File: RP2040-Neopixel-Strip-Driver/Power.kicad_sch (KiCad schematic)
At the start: 0 parts

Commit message: Moved USB and 3.3V Regulator from RP2040 to Power Sheet
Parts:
- added C?: 10uF, Breadstick Footprints:Perfect_0402_Cap, symbol Device:C_Small
- added D? (x2): ESD_TVS, Breadstick Footprints:Perfect_0402_Resistor, symbol Device:D_TVS_Filled
- added F?: 1.5A, 3A Trip, Resistor_SMD:R_0805_2012Metric, symbol Device:Polyfuse
- added J?: TYPE-C-31-M-12, TYPE-C-31-M-12:HRO_TYPE-C-31-M-12, symbol TYPE-C-31-M-12:TYPE-C-31-M-12
- added R? (x2): 5k1, Breadstick Footprints:Perfect_0402_Resistor, symbol Device:R
- added U?: XC6206P332MR, Package_TO_SOT_SMD:SOT-23, symbol BreadstickLibrary:AZ1117R-3.3TRE1
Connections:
- new net: D?.2 (A2), D?.2 (A2), F?.2, J?.A4B9 (VBUS), J?.B4A9 (VBUS)
- new net: J?.S1 (SHIELD), J?.S2 (SHIELD), J?.S3 (SHIELD), J?.S4 (SHIELD)
- new net +3V3: U?.2 (OUT)
- new net CC1: J?.A5 (CC1), R?.2
- new net CC2: J?.B5 (CC2), R?.1
- new net GND: C?.2, D?.1 (A1), D?.1 (A1), J?.A1B12 (GND), J?.B1A12 (GND), R?.1, R?.2, U?.1 (GND)
- new net USB_D+: J?.A6 (DP1), J?.B6 (DP2)
- new net USB_D-: J?.A7 (DN1), J?.B7 (DN2)
- new net VBUS: C?.1, F?.1, U?.3 (IN)
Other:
- note added: "Placed close to uC decoupling caps."
- note added: "USB-C"

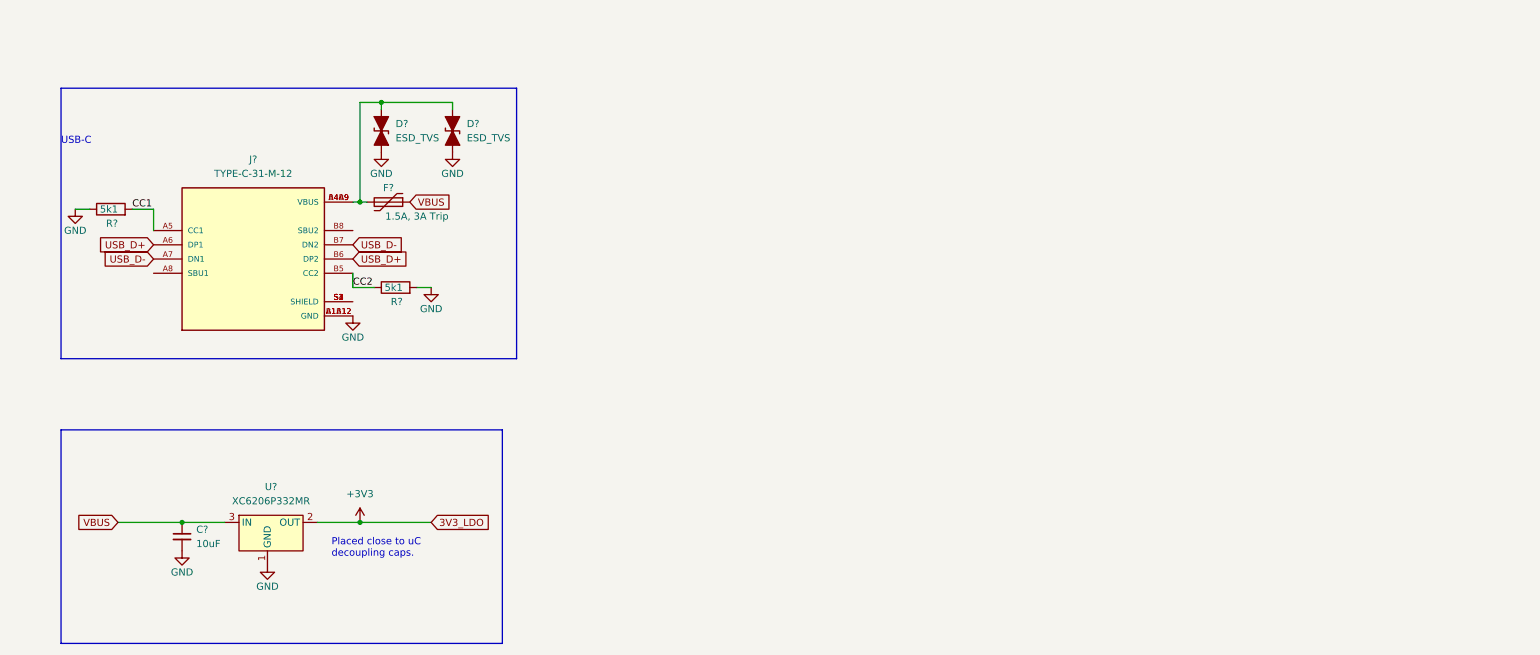
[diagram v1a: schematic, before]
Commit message: Reworked the USB-C Connector Symbol to clean up schematic
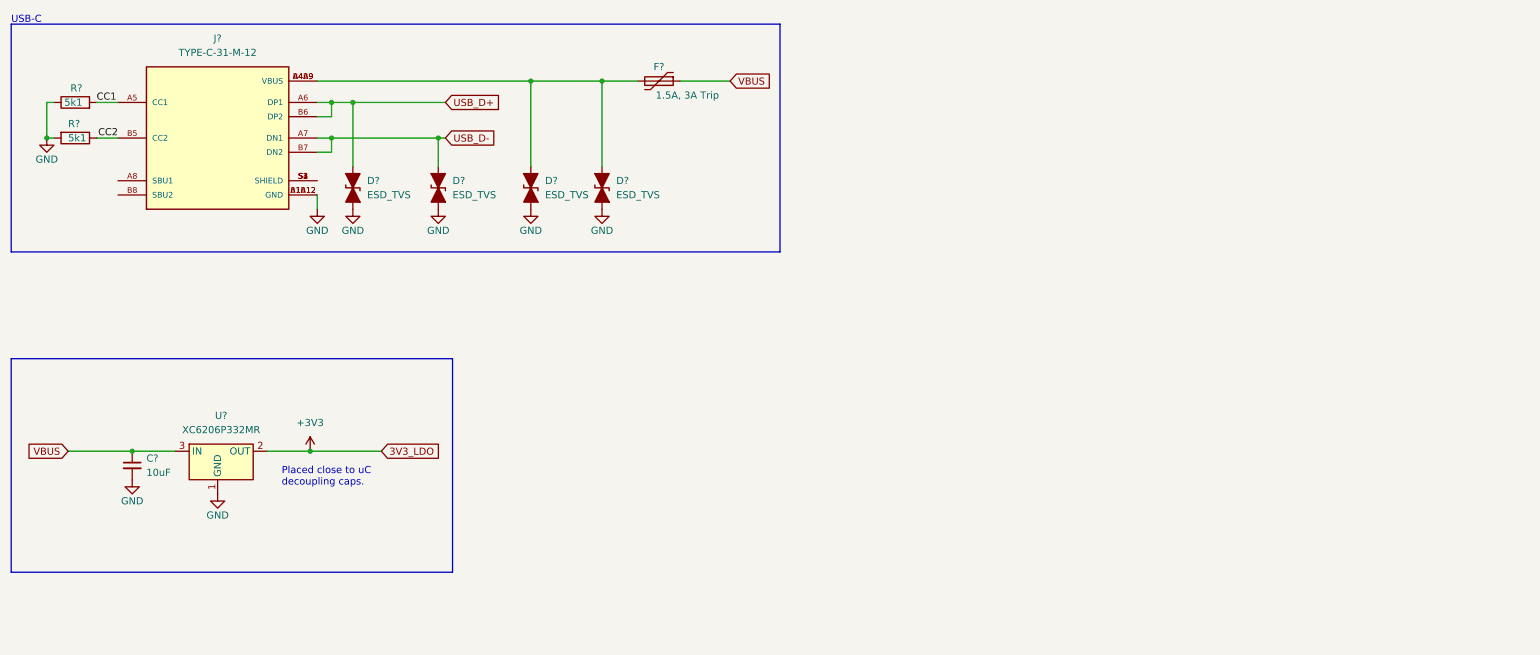
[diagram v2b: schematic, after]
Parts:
- added D? (x2): ESD_TVS, Breadstick Footprints:Perfect_0402_Resistor, symbol Device:D_TVS_Filled
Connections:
- net GND: now also D?.1 (A1), D?.1 (A1)
- net USB_D+: now also D?.2 (A2)
- net USB_D-: now also D?.2 (A2)
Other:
- moved on the sheet: C?, D?, F?, J?, R?, U?

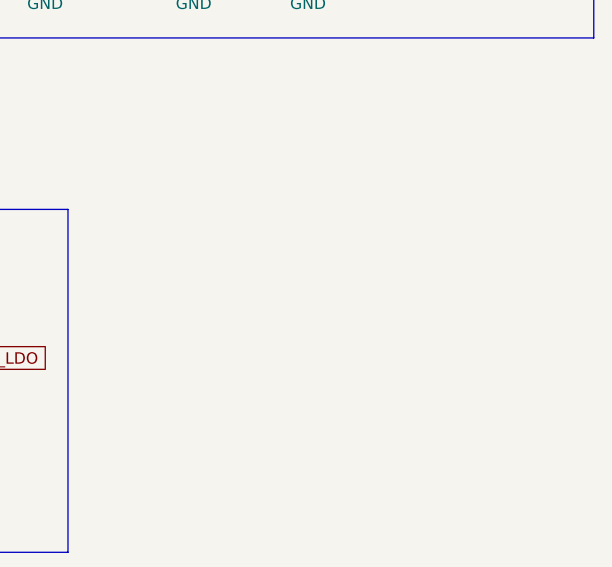
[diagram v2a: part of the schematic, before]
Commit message: Removed unnecessary pwr and gnd pins, moved decoupling caps to power sheet
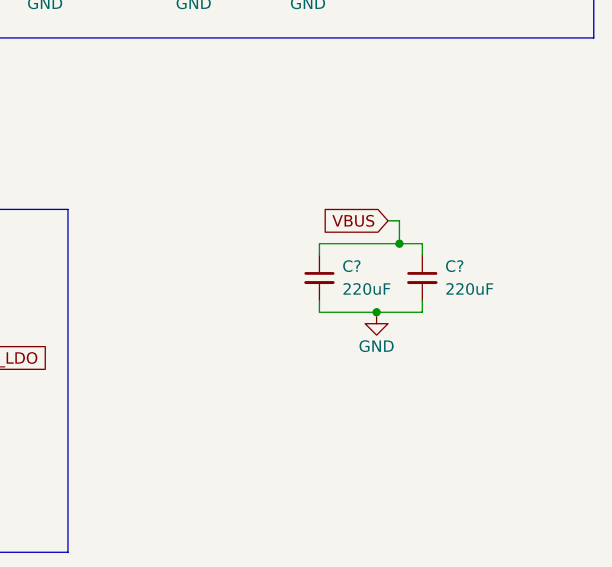
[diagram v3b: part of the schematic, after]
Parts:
- added C? (x2): 220uF, Capacitor_SMD:C_1210_3225Metric, symbol Device:C_Small
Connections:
- net GND: now also C?.2, C?.2
- net VBUS: now also C?.1, C?.1
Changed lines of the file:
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@@
   (junction (at 91.44 38.1) (diameter 0) (color 0 0 0 0)
   )
+  (junction (at 130.81 81.28) (diameter 0) (color 0 0 0 0)
+  )
+  (junction (at 128.27 88.9) (diameter 0) (color 0 0 0 0)
+  )
   (junction (at 21.59 38.1) (diameter 0) (color 0 0 0 0)
   )
@@
     (stroke (width 0) (type default) (color 0 0 0 0))
   )
+  (wire (pts (xy 130.81 81.28) (xy 133.35 81.28))
+    (stroke (width 0) (type default) (color 0 0 0 0))
+  )
   (wire (pts (xy 21.59 38.1) (xy 22.86 38.1))
     (stroke (width 0) (type default) (color 0 0 0 0))
@@
     (stroke (width 0) (type default) (color 0 0 0 0))
   )
+  (wire (pts (xy 133.35 81.28) (xy 133.35 82.55))
+    (stroke (width 0) (type default) (color 0 0 0 0))
+  )
   (wire (pts (xy 107.95 27.94) (xy 120.65 27.94))
     (stroke (width 0) (type default) (color 0 0 0 0))
@@
     (stroke (width 0) (type default) (color 0 0 0 0))
   )
+  (wire (pts (xy 121.92 87.63) (xy 121.92 88.9))
+    (stroke (width 0) (type default) (color 0 0 0 0))
+  )
   (wire (pts (xy 69.85 40.64) (xy 72.39 40.64))
     (stroke (width 0) (type default) (color 0 0 0 0))
   )
+  (wire (pts (xy 133.35 87.63) (xy 133.35 88.9))
+    (stroke (width 0) (type default) (color 0 0 0 0))
+  )
   (wire (pts (xy 30.48 31.75) (xy 34.29 31.75))
     (stroke (width 0) (type default) (color 0 0 0 0))
@@
     (stroke (width 0) (type default) (color 0 0 0 0))
   )
+  (wire (pts (xy 121.92 82.55) (xy 121.92 81.28))
+    (stroke (width 0) (type default) (color 0 0 0 0))
+  )
   (polyline (pts (xy 152.4 58.42) (xy 152.4 17.78))
     (stroke (width 0) (type default) (color 0 0 0 0))
@@
     (stroke (width 0) (type default) (color 0 0 0 0))
   )
+  (wire (pts (xy 128.27 88.9) (xy 133.35 88.9))
+    (stroke (width 0) (type default) (color 0 0 0 0))
+  )
   (wire (pts (xy 72.39 38.1) (xy 69.85 38.1))
+    (stroke (width 0) (type default) (color 0 0 0 0))
+  )
+  (wire (pts (xy 129.54 78.74) (xy 130.81 78.74))
+    (stroke (width 0) (type default) (color 0 0 0 0))
+  )
+  (wire (pts (xy 121.92 81.28) (xy 130.81 81.28))
+    (stroke (width 0) (type default) (color 0 0 0 0))
+  )
+  (wire (pts (xy 121.92 88.9) (xy 128.27 88.9))
+    (stroke (width 0) (type default) (color 0 0 0 0))
+  )
+  (wire (pts (xy 130.81 78.74) (xy 130.81 81.28))
     (stroke (width 0) (type default) (color 0 0 0 0))
   )
@@
     )
   )
+  (global_label "VBUS" (shape input) (at 129.54 78.74 180) (fields_autoplaced)
+    (effects (font (size 1.27 1.27)) (justify right))
+    (property "Intersheet References" "${INTERSHEET_REFS}" (id 0) (at 122.2283 78.8194 0)
+      (effects (font (size 1.27 1.27)) (justify right) hide)
+    )
+  )
   (global_label "USB_D-" (shape input) (at 92.71 38.1 0) (fields_autoplaced)
     (effects (font (size 1.27 1.27)) (justify left))
@@
     (pin "1")
   )
+  (symbol (lib_id "Device:C_Small") (at 121.92 85.09 0) (unit 1)
+    (in_bom yes) (on_board yes)
+    (property "Reference" "C?" (id 0) (at 124.46 83.82 0)
+      (effects (font (size 1.27 1.27)) (justify left))
+    )
+    (property "Value" "220uF" (id 1) (at 124.46 86.36 0)
+      (effects (font (size 1.27 1.27)) (justify left))
+    )
+    (property "Footprint" "Capacitor_SMD:C_1210_3225Metric" (id 2) (at 121.92 85.09 0)
+      (effects (font (size 1.27 1.27)) hide)
+    )
+    (property "Datasheet" "~" (id 3) (at 121.92 85.09 0)
+      (effects (font (size 1.27 1.27)) hide)
+    )
+    (property "JLCPCB P/N" "C400951" (id 4) (at 121.92 85.09 0)
+      (effects (font (size 1.27 1.27)) hide)
+    )
+    (pin "1")
+    (pin "2")
+  )
   (symbol (lib_id "Device:C_Small") (at 36.83 96.52 0) (unit 1)
     (in_bom yes) (on_board yes)
@@
     (pin "1")
     (pin "2")
+  )
+  (symbol (lib_id "power:GND") (at 128.27 88.9 0) (unit 1)
+    (in_bom yes) (on_board yes)
+    (property "Reference" "#PWR?" (id 0) (at 128.27 95.25 0)
+      (effects (font (size 1.27 1.27)) hide)
+    )
+    (property "Value" "GND" (id 1) (at 128.27 92.71 0))
+    (property "Footprint" "" (id 2) (at 128.27 88.9 0)
+      (effects (font (size 1.27 1.27)) hide)
+    )
+    (property "Datasheet" "" (id 3) (at 128.27 88.9 0)
+      (effects (font (size 1.27 1.27)) hide)
+    )
+    (pin "1")
   )
   (symbol (lib_id "Device:Polyfuse") (at 130.81 27.94 270) (unit 1)
@@
     (pin "1")
   )
+  (symbol (lib_id "Device:C_Small") (at 133.35 85.09 0) (unit 1)
+    (in_bom yes) (on_board yes)
+    (property "Reference" "C?" (id 0) (at 135.89 83.82 0)
+      (effects (font (size 1.27 1.27)) (justify left))
+    )
+    (property "Value" "220uF" (id 1) (at 135.89 86.36 0)
+      (effects (font (size 1.27 1.27)) (justify left))
+    )
+    (property "Footprint" "Capacitor_SMD:C_1210_3225Metric" (id 2) (at 133.35 85.09 0)
+      (effects (font (size 1.27 1.27)) hide)
+    )
+    (property "Datasheet" "~" (id 3) (at 133.35 85.09 0)
+      (effects (font (size 1.27 1.27)) hide)
+    )
+    (property "JLCPCB P/N" "C400951" (id 4) (at 133.35 85.09 0)
+      (effects (font (size 1.27 1.27)) hide)
+    )
+    (pin "1")
+    (pin "2")
+  )
   (symbol (lib_id "Device:D_TVS_Filled") (at 76.2 46.99 90) (unit 1)

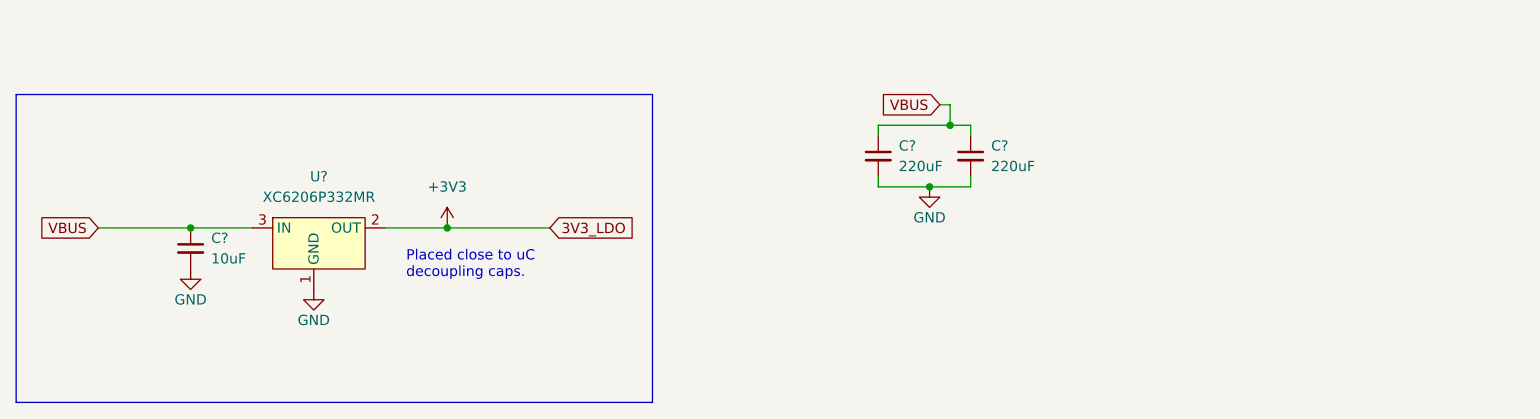
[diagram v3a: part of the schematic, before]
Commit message: Found diode for power supply ORing
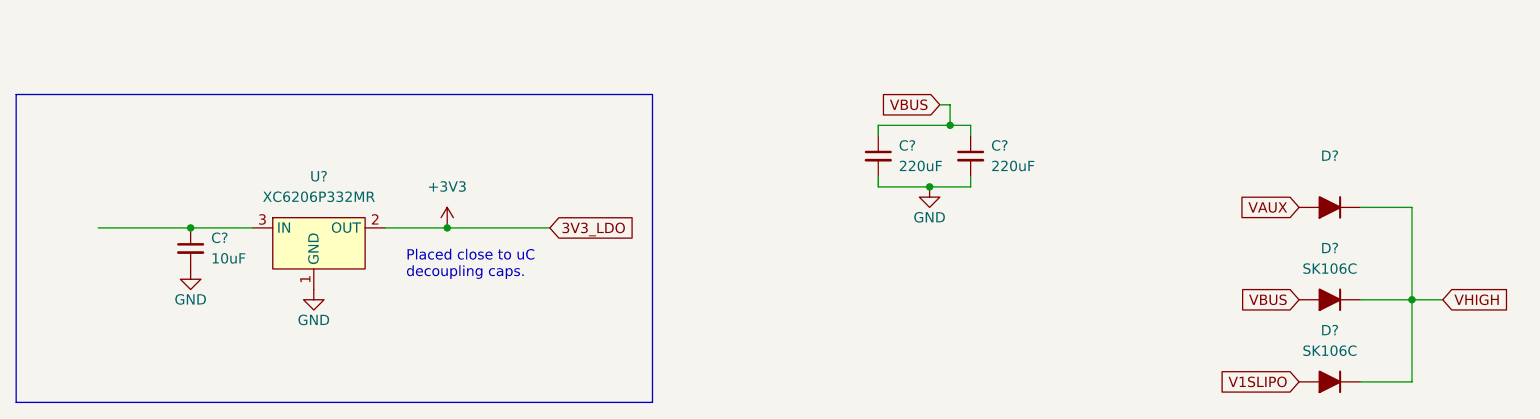
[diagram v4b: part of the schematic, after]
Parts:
- added D?: (no value), symbol Device:D_Filled
- added D? (x2): SK106C, Diode_SMD:D_SMC, symbol Device:D_Filled
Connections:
- net VBUS: now also D?.2 (A); no longer C?.1, U?.3 (IN)
- new net: C?.1, U?.3 (IN)
- new net V1SLIPO: D?.2 (A)
- new net VAUX: D?.2 (A)
- new net VHIGH: D?.1 (K), D?.1 (K), D?.1 (K)
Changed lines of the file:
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@@
   (junction (at 107.95 27.94) (diameter 0) (color 0 0 0 0)
   )
+  (junction (at 187.96 102.87) (diameter 0) (color 0 0 0 0)
+  )
+  (wire (pts (xy 187.96 91.44) (xy 181.61 91.44))
+    (stroke (width 0) (type default) (color 0 0 0 0))
+  )
   (wire (pts (xy 76.2 31.75) (xy 76.2 43.18))
     (stroke (width 0) (type default) (color 0 0 0 0))
@@
     (stroke (width 0) (type default) (color 0 0 0 0))
   )
+  (wire (pts (xy 187.96 102.87) (xy 191.77 102.87))
+    (stroke (width 0) (type default) (color 0 0 0 0))
+  )
   (wire (pts (xy 34.29 38.1) (xy 30.48 38.1))
     (stroke (width 0) (type default) (color 0 0 0 0))
@@
     (stroke (width 0) (type default) (color 0 0 0 0))
   )
+  (wire (pts (xy 181.61 102.87) (xy 187.96 102.87))
+    (stroke (width 0) (type default) (color 0 0 0 0))
+  )
   (wire (pts (xy 121.92 82.55) (xy 121.92 81.28))
     (stroke (width 0) (type default) (color 0 0 0 0))
@@
     (stroke (width 0) (type default) (color 0 0 0 0))
   )
+  (wire (pts (xy 187.96 113.03) (xy 187.96 102.87))
+    (stroke (width 0) (type default) (color 0 0 0 0))
+  )
   (wire (pts (xy 134.62 27.94) (xy 143.51 27.94))
     (stroke (width 0) (type default) (color 0 0 0 0))
@@
     (stroke (width 0) (type default) (color 0 0 0 0))
   )
+  (wire (pts (xy 187.96 102.87) (xy 187.96 91.44))
+    (stroke (width 0) (type default) (color 0 0 0 0))
+  )
   (wire (pts (xy 130.81 78.74) (xy 130.81 81.28))
     (stroke (width 0) (type default) (color 0 0 0 0))
@@
   )
   (polyline (pts (xy 15.24 77.47) (xy 93.98 77.47))
+    (stroke (width 0) (type default) (color 0 0 0 0))
+  )
+  (wire (pts (xy 181.61 113.03) (xy 187.96 113.03))
     (stroke (width 0) (type default) (color 0 0 0 0))
   )
@@
     (effects (font (size 1.27 1.27)) (justify right bottom))
   )
-  (global_label "VBUS" (shape input) (at 25.4 93.98 180) (fields_autoplaced)
+  (global_label "VHIGH" (shape input) (at 191.77 102.87 0) (fields_autoplaced)
+    (effects (font (size 1.27 1.27)) (justify left))
+    (property "Intersheet References" "${INTERSHEET_REFS}" (id 0) (at 199.8074 102.7906 0)
+      (effects (font (size 1.27 1.27)) (justify left) hide)
+    )
+  )
+  (global_label "VBUS" (shape input) (at 173.99 102.87 180) (fields_autoplaced)
     (effects (font (size 1.27 1.27)) (justify right))
-    (property "Intersheet References" "${INTERSHEET_REFS}" (id 0) (at 18.0883 94.0594 0)
+    (property "Intersheet References" "${INTERSHEET_REFS}" (id 0) (at 166.6783 102.9494 0)
+      (effects (font (size 1.27 1.27)) (justify right) hide)
+    )
+  )
+  (global_label "V1SLIPO" (shape input) (at 173.99 113.03 180) (fields_autoplaced)
+    (effects (font (size 1.27 1.27)) (justify right))
+    (property "Intersheet References" "${INTERSHEET_REFS}" (id 0) (at 163.8359 112.9506 0)
+      (effects (font (size 1.27 1.27)) (justify right) hide)
+    )
+  )
+  (global_label "VAUX" (shape input) (at 173.99 91.44 180) (fields_autoplaced)
+    (effects (font (size 1.27 1.27)) (justify right))
+    (property "Intersheet References" "${INTERSHEET_REFS}" (id 0) (at 166.8598 91.3606 0)
       (effects (font (size 1.27 1.27)) (justify right) hide)
     )
@@
     (pin "1")
   )
+  (symbol (lib_id "Device:D_Filled") (at 177.8 91.44 180) (unit 1)
+    (in_bom yes) (on_board yes) (fields_autoplaced)
+    (property "Reference" "D?" (id 0) (at 177.8 85.09 0))
+    (property "Value" "" (id 1) (at 177.8 87.63 0))
+    (property "Footprint" "" (id 2) (at 177.8 91.44 0)
+      (effects (font (size 1.27 1.27)) hide)
+    )
+    (property "Datasheet" "~" (id 3) (at 177.8 91.44 0)
+      (effects (font (size 1.27 1.27)) hide)
+    )
+    (property "JLCPCB P/N" "C65019" (id 4) (at 177.8 91.44 0)
+      (effects (font (size 1.27 1.27)) hide)
+    )
+    (pin "1")
+    (pin "2")
+  )
   (symbol (lib_id "Device:C_Small") (at 121.92 85.09 0) (unit 1)
     (in_bom yes) (on_board yes)
@@
     )
     (property "JLCPCB P/N" "C15525" (id 4) (at 36.83 96.52 0)
+      (effects (font (size 1.27 1.27)) hide)
+    )
+    (pin "1")
+    (pin "2")
+  )
+  (symbol (lib_id "Device:D_Filled") (at 177.8 102.87 180) (unit 1)
+    (in_bom yes) (on_board yes) (fields_autoplaced)
+    (property "Reference" "D?" (id 0) (at 177.8 96.52 0))
+    (property "Value" "SK106C" (id 1) (at 177.8 99.06 0))
+    (property "Footprint" "Diode_SMD:D_SMC" (id 2) (at 177.8 102.87 0)
+      (effects (font (size 1.27 1.27)) hide)
+    )
+    (property "Datasheet" "~" (id 3) (at 177.8 102.87 0)
+      (effects (font (size 1.27 1.27)) hide)
+    )
+    (property "JLCPCB P/N" "C65019" (id 4) (at 177.8 102.87 0)
       (effects (font (size 1.27 1.27)) hide)
     )
@@
     (pin "S4")
   )
+  (symbol (lib_id "Device:D_Filled") (at 177.8 113.03 180) (unit 1)
+    (in_bom yes) (on_board yes) (fields_autoplaced)
+    (property "Reference" "D?" (id 0) (at 177.8 106.68 0))
+    (property "Value" "SK106C" (id 1) (at 177.8 109.22 0))
+    (property "Footprint" "Diode_SMD:D_SMC" (id 2) (at 177.8 113.03 0)
+      (effects (font (size 1.27 1.27)) hide)
+    )
+    (property "Datasheet" "~" (id 3) (at 177.8 113.03 0)
+      (effects (font (size 1.27 1.27)) hide)
+    )
+    (property "JLCPCB P/N" "C65019" (id 4) (at 177.8 113.03 0)
+      (effects (font (size 1.27 1.27)) hide)
+    )
+    (pin "1")
+    (pin "2")
+  )
   (symbol (lib_id "power:GND") (at 107.95 50.8 0) (unit 1)

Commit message: Added Pico W
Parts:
- D?: value (none) -> SK106C; footprint (none) -> Diode_SMD:D_SMC
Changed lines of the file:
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@@
     (in_bom yes) (on_board yes) (fields_autoplaced)
     (property "Reference" "D?" (id 0) (at 177.8 85.09 0))
-    (property "Value" "" (id 1) (at 177.8 87.63 0))
-    (property "Footprint" "" (id 2) (at 177.8 91.44 0)
+    (property "Value" "SK106C" (id 1) (at 177.8 87.63 0))
+    (property "Footprint" "Diode_SMD:D_SMC" (id 2) (at 177.8 91.44 0)
       (effects (font (size 1.27 1.27)) hide)
     )
